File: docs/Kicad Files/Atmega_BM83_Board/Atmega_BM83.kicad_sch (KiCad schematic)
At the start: 32 parts, among them J1 18V, J2 Out to Amp, J3 PWR SW, J4 Volume POT, J5 Pairing BTN, J6 PWR LED, J7 Pair LED, J8 Conn_01x12, J9 Conn_01x12, U1 LF353N, U2 LM7805_TO220, U3 ATmega328P-P

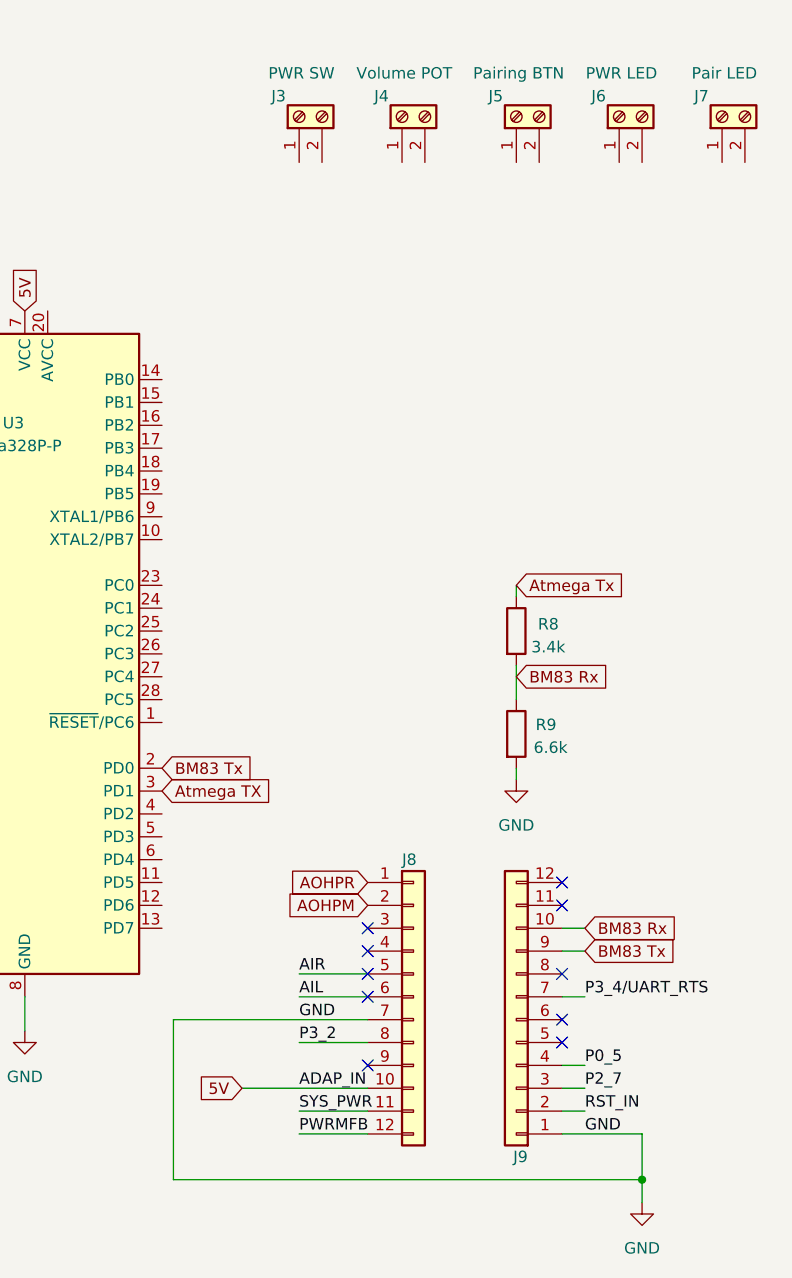
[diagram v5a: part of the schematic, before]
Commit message: updates to BM83/MC schematic
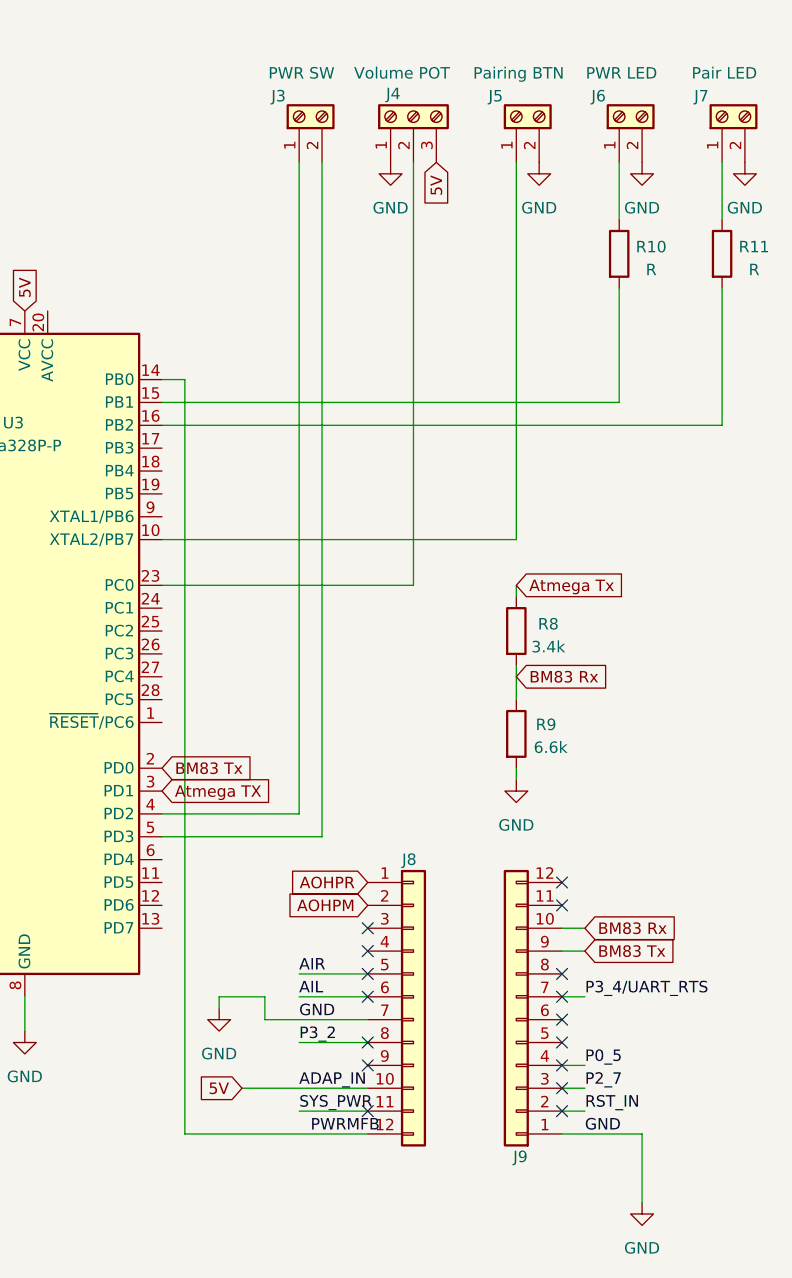
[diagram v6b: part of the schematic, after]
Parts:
- removed J4: Volume POT, TerminalBlock_Phoenix:TerminalBlock_Phoenix_MKDS-1,5-2_1x02_P5.00mm_Horizontal, symbol Connector:Screw_Terminal_01x02
- added J4: Volume POT, symbol Connector:Screw_Terminal_01x03
- added R10, R11: R, Resistor_THT:R_Axial_DIN0207_L6.3mm_D2.5mm_P10.16mm_Horizontal, symbol Device:R
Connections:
- net 5V: now also J4.3 (Pin_3)
- net GND: now also J5.2 (Pin_2), J6.2 (Pin_2), J7.2 (Pin_2), J4.1 (Pin_1)
- net PWRMFB: now also U3.14 (PB0)
- net at J7.1 (Pin_1): now also R11.1
- net at J6.1 (Pin_1): now also R10.1
- net at J3.1 (Pin_1): now also U3.4 (PD2)
- net at J3.2 (Pin_2): now also U3.5 (PD3)
- net at J5.1 (Pin_1): now also U3.10 (XTAL2/PB7)
- net at U3.15 (PB1): now also R10.2
- net at U3.16 (PB2): now also R11.2
- net at U3.23 (PC0): now also J4.2 (Pin_2)
- no-connect marks 10 -> 16

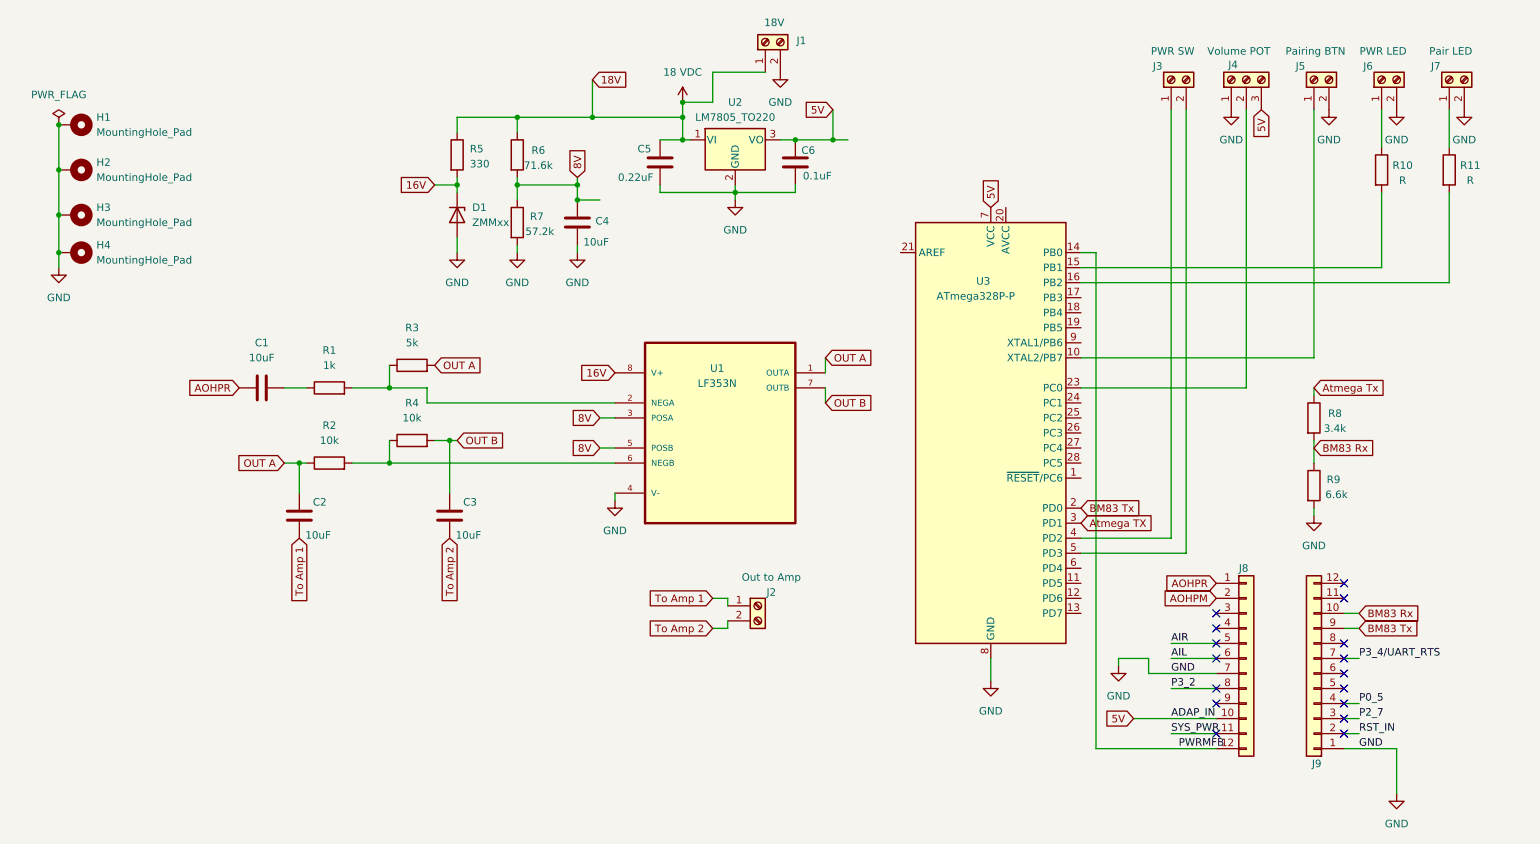
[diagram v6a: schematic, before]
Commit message: added ICE header and other connections to BM83/MC schematic
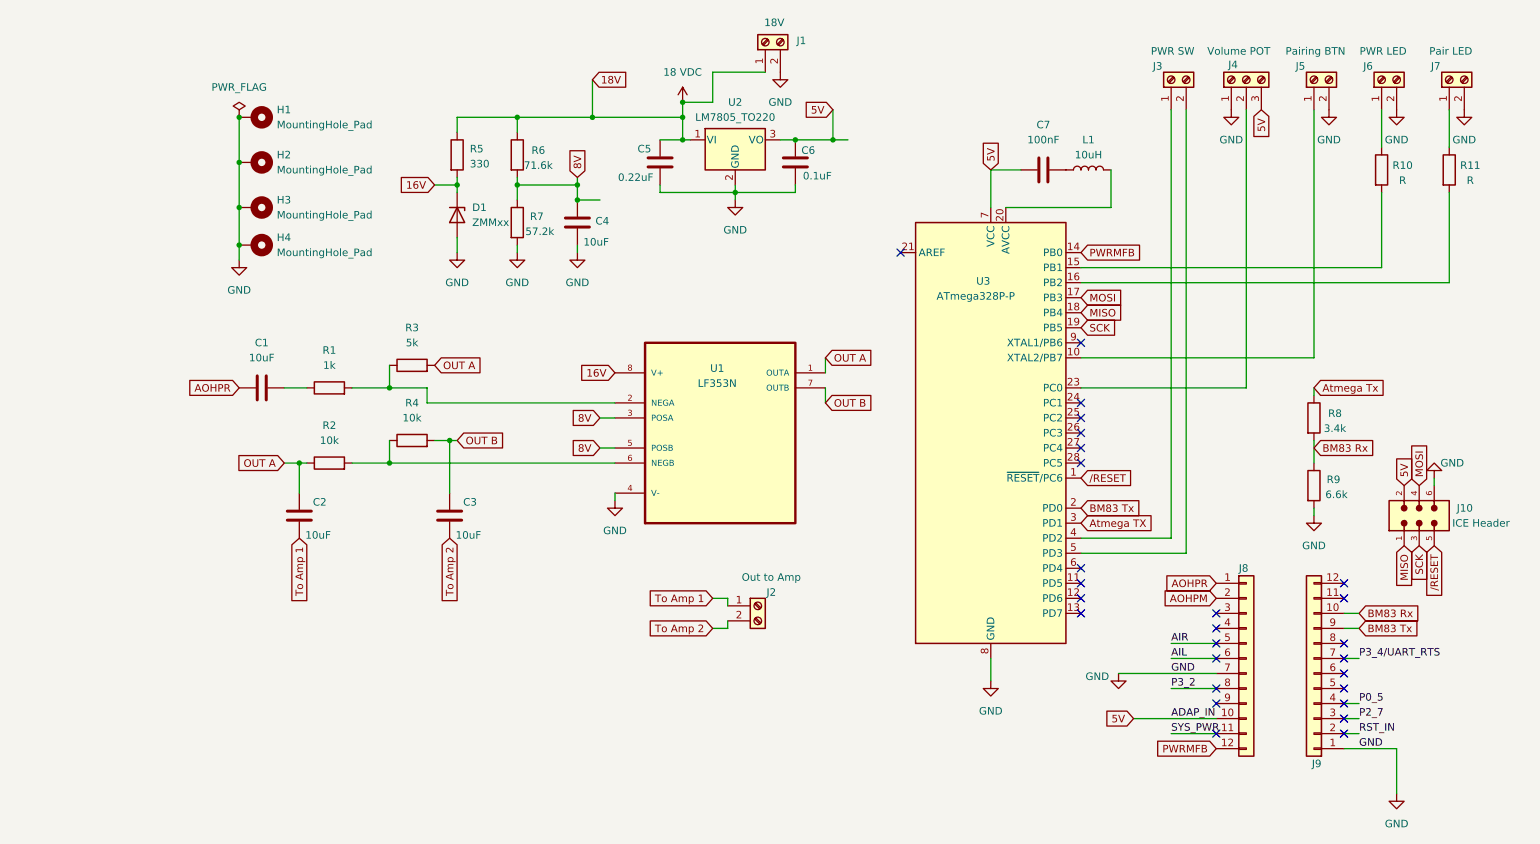
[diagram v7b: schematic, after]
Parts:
- added C7: 100nF, symbol Device:C
- added J10: ICE Header, 6120XX21621_61200621621:61200621621, symbol ICE_Header:6120XX21621_61200621621
- added L1: 10uH, symbol Device:L
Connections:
- net 5V: now also C7.1, J10.2
- net GND: now also J10.6
- net /RESET: now reaches U3.1 (~{RESET}/PC6)
- net /RESET: now also J10.5
- net MOSI: now reaches U3.17 (PB3)
- net MOSI: now also J10.4
- net MISO: now reaches U3.18 (PB4)
- net MISO: now also J10.1
- net SCK: now reaches U3.19 (PB5)
- net SCK: now also J10.3
- net at U3.20 (AVCC): now also L1.2
- new net: C7.2, L1.1
- no-connect marks 16 -> 27
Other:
- moved on the sheet: H1, H2, H3, H4

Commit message: op-amp changes to MC/BM83 schematic
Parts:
- removed D1: ZMMxx, Diode_SMD:D_MiniMELF, symbol Diode:ZMMxx
- removed L1: 10uH, symbol Device:L
- removed R5: 330, Resistor_THT:R_Axial_DIN0207_L6.3mm_D2.5mm_P10.16mm_Horizontal, symbol Device:R
- removed U1: LF353N, Z_Custom_Footprints:LF353, symbol LF353N:LF353N
- added U4: LF353N, Package_DIP:DIP-8_W7.62mm_LongPads, symbol Amplifier_Operational:TL082
- C7: value 100nF -> 0.1uF
- J10: footprint 6120XX21621_61200621621:61200621621 -> Z_Custom_Footprints:ICE_Header
- J4: footprint (none) -> TerminalBlock_Phoenix:TerminalBlock_Phoenix_MKDS-1,5-3-5.08_1x03_P5.08mm_Horizontal
- R2: renamed from R3; value 5k -> 4.7k
- U3: footprint Package_DIP:DIP-28_W7.62mm -> Package_DIP:DIP-28_W7.62mm_LongPads
- renumbered R2 to R3
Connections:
- net 18 VDC: now also U4.8 (V+)
- net 5V: now also J6.2 (Pin_2), J7.2 (Pin_2); no longer C7.1
- net 8V: now also U4.3 (+), U4.5 (+)
- net GND: now also C7.1, U4.4 (V-); no longer J6.2 (Pin_2), J7.2 (Pin_2)
- net at R3.2: now also C2.2, R2.2, U4.1; no longer R4.1
- net at R1.2, R2.1: now also U4.2 (-)
- net at C7.2: now also U3.20 (AVCC)
- removed net OUT A: C2.2, R2.2, R3.1
- net OUT B: no longer names the net of C3.2, R4.2
- net OUT B: now also U4.7
- net To Amp 1: no longer names the net of C2.1, J2.1 (Pin_1)
- net To Amp 2: no longer names the net of C3.1, J2.2 (Pin_2)
- new net: R3.1, R4.1, U4.6 (-)
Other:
- moved on the sheet: C1, C2, C3, C7, J2, R1, R2, R3
